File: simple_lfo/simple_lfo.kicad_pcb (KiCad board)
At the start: 2 copper layers, 49.5 x 128.5 mm, 33 parts, among them J1 LFO Out, J2 Power Connector, SW1 Range, SW2 Waveform, U1 TL074

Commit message: LFO: All components on pcbs laid out
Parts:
- added J1: To J3, Connector_PinSocket_2.54mm:PinSocket_1x03_P2.54mm_Vertical, B.Cu at (182.5, 59.5)
- added J10: To J4 (Range Switch), Connector_PinHeader_2.54mm:PinHeader_1x03_P2.54mm_Vertical, F.Cu at (227.5, 88.5)
- added J11: To J3, Connector_PinSocket_2.54mm:PinSocket_1x03_P2.54mm_Vertical, B.Cu at (197.5, 88.5)
- added J2: Conn_01x03_Pin, Connector_PinHeader_2.54mm:PinHeader_1x03_P2.54mm_Vertical, F.Cu at (212.5, 59.5)
- added J3: To J4 (Range Switch), Connector_PinHeader_2.54mm:PinHeader_1x03_P2.54mm_Vertical, F.Cu at (227.5, 59.5)
- added J4: To J3, Connector_PinSocket_2.54mm:PinSocket_1x03_P2.54mm_Vertical, B.Cu at (197.5, 59.5)
- added J5: To J4 (Range Switch), Connector_PinHeader_2.54mm:PinHeader_1x03_P2.54mm_Vertical, F.Cu at (212.5, 88.5)
- added J6: To J3, Connector_PinSocket_2.54mm:PinSocket_1x03_P2.54mm_Vertical, B.Cu at (182.5, 88.5)
- added J7: To J4 (Range Switch), Connector_PinHeader_2.54mm:PinHeader_1x03_P2.54mm_Vertical, F.Cu at (227.5, 113.5)
- added J8: To J3, Connector_PinSocket_2.54mm:PinSocket_1x03_P2.54mm_Vertical, B.Cu at (197.5, 113.5)
- C3, C4: moved to B.Cu
- moved R10 203.4 mm to (227.5, 68.0), turned to -90 degrees
- moved R9 201.7 mm to (222.5, 93.3), turned to -90 degrees
- moved R7 200.6 mm to (223.5, 71.0), turned to 90 degrees
- moved R8 196.7 mm to (220.0, 71.0), turned to 90 degrees
- moved R6 194.1 mm to (216.5, 71.0), turned to 90 degrees
- moved R5 193.3 mm to (217.5, 45.0), turned to -90 degrees
- moved R3 192.9 mm to (212.5, 74.0), turned to -90 degrees
- moved R2 190.8 mm to (214.5, 41.5)
- moved R4 189.2 mm to (212.5, 55.0), turned to 90 degrees
- moved C8 180.1 mm to (227.5, 102.5), turned to 90 degrees
- moved C7 165.3 mm to (212.5, 97.5), turned to -90 degrees
- moved R1 137.8 mm to (212.0, 38.0)
- moved C5 131.2 mm to (222.5, 108.5)
- moved R11 126.0 mm to (217.0, 127.5), turned to 90 degrees
- moved C6 126.0 mm to (217.5, 106.0), turned to 180 degrees
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- renumbered J2 to J12, J1 to J9
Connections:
- C1 pad 2: Net-(SW1-A) -> Net-(J3-Pin_1)
- C2 pad 2: Net-(SW1-C) -> Net-(J3-Pin_2)
- J9 pad S: GND -> CTRL_PANEL_GND
- J9 pad T: Net-(U1C--) -> Net-(J8-Pin_2)
- J9 pad TN: GND -> CTRL_PANEL_GND
- R1 pad 1: Net-(R1-Pad1) -> Net-(J2-Pin_3)
- R10 pad 2: Net-(D1-AK) -> Net-(J10-Pin_2)
- R2 pad 1: Net-(R2-Pad1) -> Net-(J2-Pin_2)
- R4 pad 2: Net-(R4-Pad2) -> Net-(J2-Pin_1)
- R5 pad 1: Net-(R4-Pad2) -> Net-(J2-Pin_1)
- R6 pad 2: Net-(R4-Pad2) -> Net-(J2-Pin_1)
- R7 pad 1: Net-(SW2-C) -> Net-(J5-Pin_2)
- R8 pad 1: Net-(SW2-C) -> Net-(J5-Pin_2)
- R9 pad 2: Net-(D1-KA) -> Net-(J10-Pin_1)
- RV1 pad 1: Net-(R1-Pad1) -> Net-(J1-Pin_3)
- RV1 pad 2: Net-(R2-Pad1) -> Net-(J1-Pin_2)
- RV1 pad 3: Net-(R4-Pad2) -> Net-(J1-Pin_1)
- RV2 pad 1: GND -> CTRL_PANEL_GND
- RV2 pad 2: Net-(U1C-+) -> Net-(J6-Pin_3)
- SW1 pad 1: Net-(SW1-A) -> Net-(J4-Pin_1)
- SW1 pad 2: LFO_Triangle -> Net-(J4-Pin_3)
- SW1 pad 3: Net-(SW1-C) -> Net-(J4-Pin_2)
- SW2 pad 1: LFO_Triangle -> Net-(J6-Pin_1)
- SW2 pad 3: Net-(SW2-C) -> Net-(J6-Pin_2)
- U1 pad 10: Net-(U1C-+) -> Net-(J5-Pin_3)
- U1 pad 12: Net-(U1C--) -> Net-(J7-Pin_2)
- U1 pad 13: Net-(D1-AK) -> Net-(J10-Pin_2)
- U1 pad 8: Net-(U1C--) -> Net-(J7-Pin_2)
- U1 pad 9: Net-(U1C--) -> Net-(J7-Pin_2)
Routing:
- net Net-(U1A--): track 0.00 -> 48.1 mm, vias 0 -> 2
- net Net-(D1-KA): track 0.00 -> 38.4 mm, vias 0 -> 2
- net Net-(D1-AK): track 0.00 -> 34.6 mm, vias 0 -> 1
- net +12V: track 0.00 -> 33.9 mm
- net -12V: track 0.00 -> 31.2 mm
- net Net-(D2-A): track 0.00 -> 28.0 mm, vias 0 -> 1
- net Net-(J2-Pin_3): track 0.00 -> 27.3 mm
- net Net-(SW2-B): track 0.00 -> 26.8 mm
- net Net-(J2-Pin_1): track 0.00 -> 25.2 mm
- net Net-(J6-Pin_3): track 0.00 -> 23.1 mm, vias 0 -> 1
- net Net-(J2-Pin_2): track 0.00 -> 21.3 mm
- net Net-(J8-Pin_2): track 0.00 -> 17.1 mm, vias 0 -> 1
- net Net-(J6-Pin_2): track 0.00 -> 16.5 mm, vias 0 -> 1
- net Net-(D3-K): track 0.00 -> 14.7 mm
- net Net-(J3-Pin_1): track 0.00 -> 14.5 mm
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- added copper zone on B.Cu, net CTRL_PANEL_GND
- added copper zone on B.Cu, net GND
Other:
- board size 49.5 x 128.5 mm -> 79.5 x 128.5 mm
- board text added: "- Flip power components so that the sides line up with TL047 power pins"
- board text removed: "- Realign panel elements with Iosevka - Split control board from logic board in schematic"

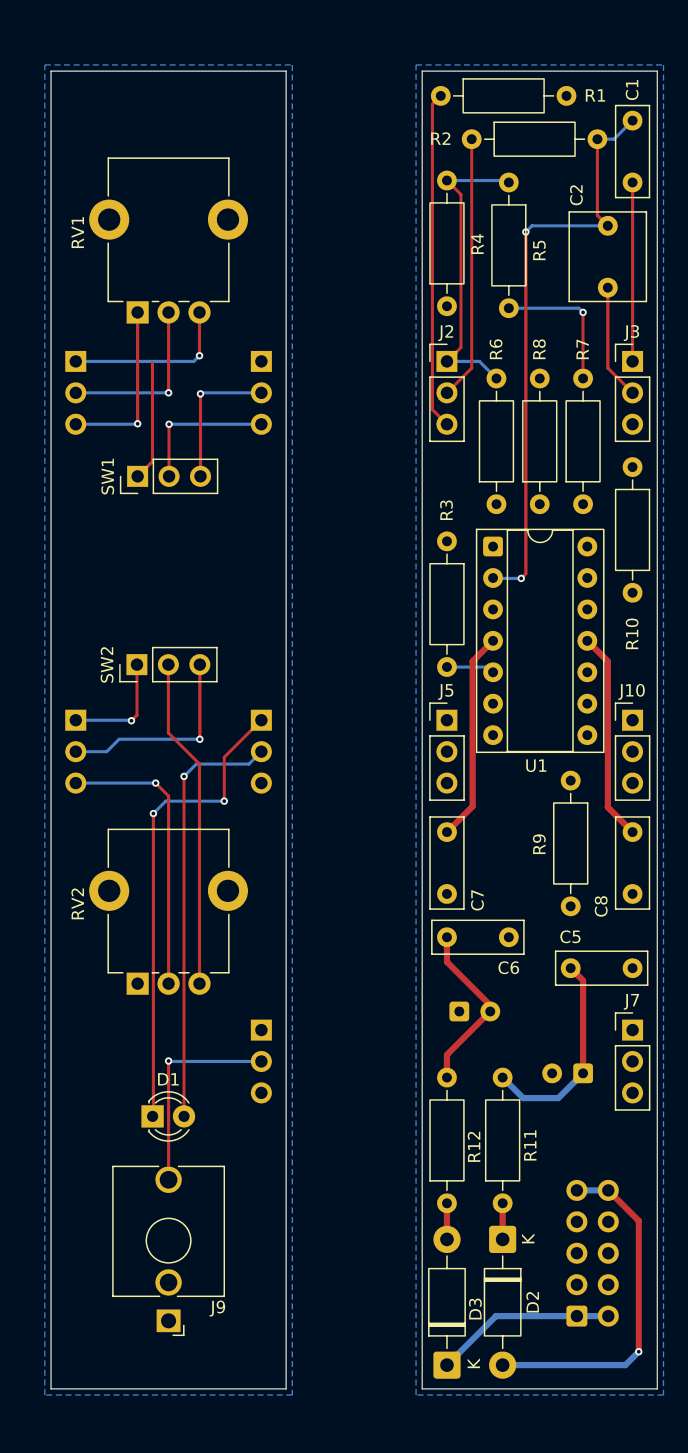
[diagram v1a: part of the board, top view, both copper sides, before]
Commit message: LFO: finish routing pcb
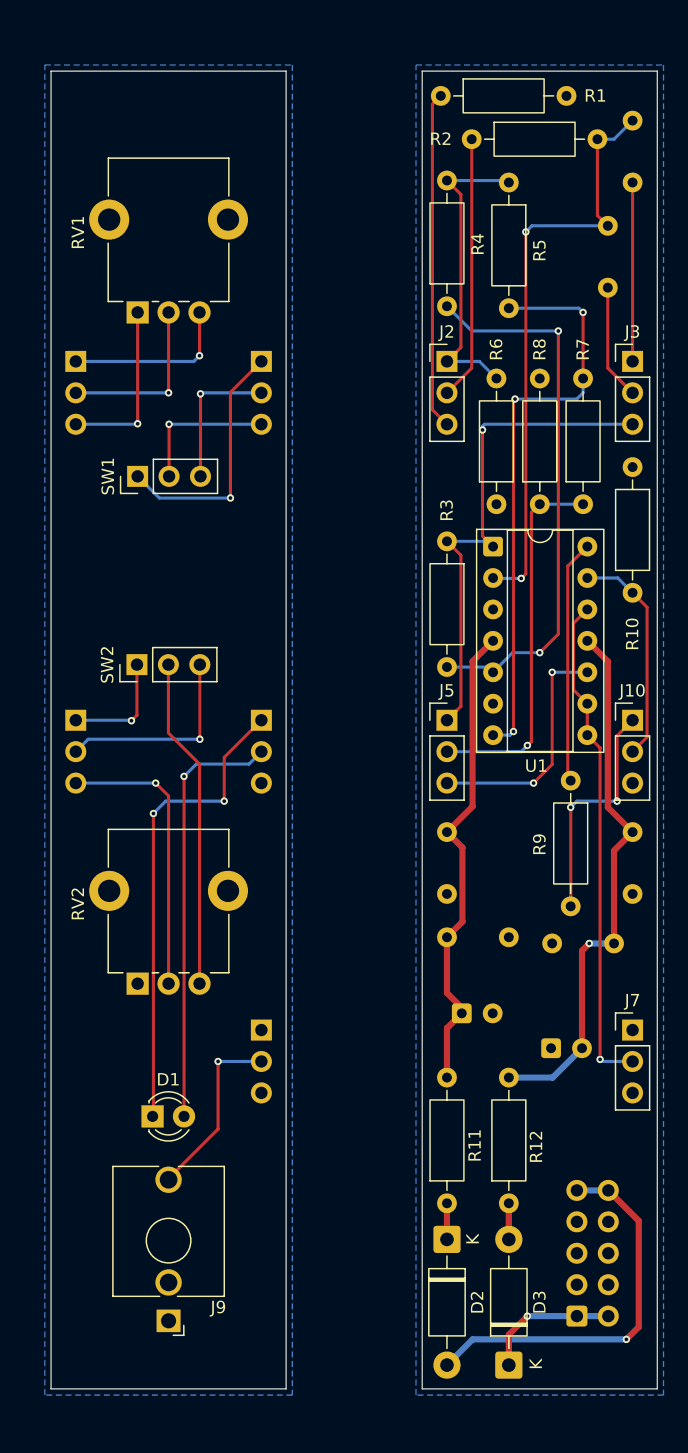
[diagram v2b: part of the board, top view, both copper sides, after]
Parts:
- C1, C2, C5, C6, C7, C8: moved to B.Cu
- moved C3 10.9 mm to (213.7, 112.1), turned to 0 degrees
- moved C5 10.3 mm to (212.5, 106.0)
- moved C4 7.99 mm to (220.9, 115.0)
- moved D3 5.00 mm to (217.5, 140.6)
- moved R12 5.00 mm to (217.5, 127.5)
- moved D2 4.50 mm to (212.5, 130.4)
- moved R11 4.50 mm to (212.5, 127.5)
- moved C6 3.54 mm to (221.0, 106.5), turned to 0 degrees
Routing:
- net LFO_Triangle: track 0.00 -> 41.6 mm, vias 0 -> 1
- net Net-(U1B-+): track 3.90 -> 44.8 mm, vias 0 -> 2
- net Net-(J7-Pin_2): track 0.00 -> 40.4 mm, vias 0 -> 1
- net LFO_Square: track 11.5 -> 47.0 mm, vias 1 -> 3
- net Net-(J5-Pin_2): track 0.00 -> 30.1 mm, vias 0 -> 1
- net Net-(R9-Pad1): track 0.00 -> 19.7 mm
- net Net-(J5-Pin_3): track 0.00 -> 19.4 mm, vias 0 -> 2
- net Net-(J10-Pin_1): track 0.00 -> 19.0 mm, vias 0 -> 2
- net Net-(J10-Pin_2): track 0.00 -> 18.0 mm
- net -12V: track 31.2 -> 44.2 mm, vias 0 -> 1
- net Net-(J4-Pin_1): track 9.67 -> 20.3 mm, vias 0 -> 1
- net +12V: track 33.9 -> 38.9 mm
- net Net-(D3-K): track 14.7 -> 11.1 mm, vias 0 -> 1
- net Net-(D2-A): track 28.0 -> 31.4 mm
- net Net-(J8-Pin_2): track 17.1 -> 14.7 mm
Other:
- board text added: "Simple LFO Control Board Rev 0 Jesse Holzman"
- board text added: "Simple LFO Main Board Rev 0 Jesse Holzman"
